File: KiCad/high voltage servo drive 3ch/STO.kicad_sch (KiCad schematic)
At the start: 34 parts, among them J8 STO, Q1 BSS83P, U15 PC-817S1-CTP1-F, U16 PC-817S1-CTP1-F, U19 PC-817S1-CTP1-F

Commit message: prepare rev0.1 for manufacturing
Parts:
- C188, C189, C190: Generic Allowed? (none) -> yes; LCSC# (none) -> C105882; Manufacturer (none) -> YAGEO; Part number (none) -> CC0402KRX5R9BB104; cost (none) -> 0.003
- D34, D38, D48: LCSC# (none) -> C12765; Manufacturer onsemi -> LRC; Part number BAT54SLT1G -> LBAT54SLT1G; cost (none) -> 0.01
- D35, D37, D49: LCSC# (none) -> C5199207; Manufacturer SMC Diode Solutions -> ElecSuper; Part number SM712 -> CDSOT23-SM712-ES; cost (none) -> 0.03
- D36: value STO_CH_1 -> LED; Generic Allowed? (none) -> yes; LCSC# (none) -> C965807; Manufacturer (none) -> XINGLIGHT; Part number (none) -> XL-1608UBC-04; cost (none) -> 0.004
- D39: value STO_CH_2 -> LED; Generic Allowed? (none) -> yes; LCSC# (none) -> C965807; Manufacturer (none) -> XINGLIGHT; Part number (none) -> XL-1608UBC-04; cost (none) -> 0.004
- D50: value STO_FBK -> LED; Generic Allowed? (none) -> yes; LCSC# (none) -> C965807; Manufacturer (none) -> XINGLIGHT; Part number (none) -> XL-1608UBC-04; cost (none) -> 0.004
- J8: now not fitted
- Q1: Generic Allowed? (none) -> yes; LCSC# (none) -> C7472872; Manufacturer (none) -> TECH PUBLIC; Part number (none) -> BSS83P; cost (none) -> 0.06
- R128, R129, R130, R131, R134, R87, R88, R89, R90, R92, R93, R94, R95: Generic Allowed? (none) -> yes, 1% or better; LCSC# (none) -> C106235; Manufacturer (none) -> YAGEO; Part number (none) -> RC0402FR-071KL; cost (none) -> 0.0007
- R132, R133, R91, R96: Generic Allowed? (none) -> yes; LCSC# (none) -> C60490; Manufacturer (none) -> YAGEO; Part number (none) -> RC0402FR-0710KL; cost (none) -> 0.0007
- U15, U16, U19: Manufacturer (none) -> HENGTUO; Part number (none) -> PC-817S1-CTP1-F; cost (none) -> 0.03

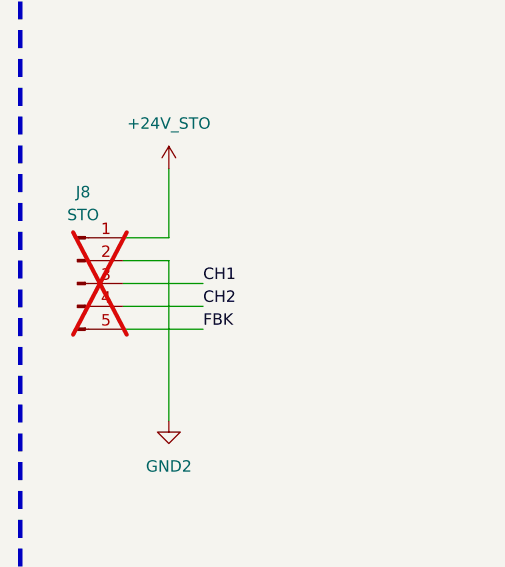
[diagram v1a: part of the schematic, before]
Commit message: update BOM and change transceivers
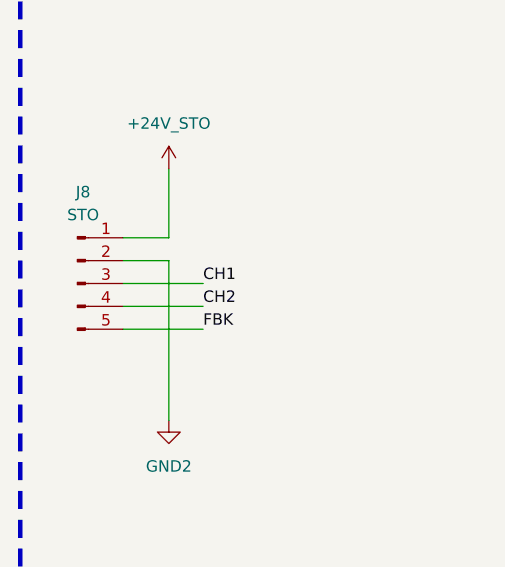
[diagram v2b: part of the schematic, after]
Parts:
- J8: now fitted
- U15, U16, U19: footprint Package_DIP:DIP-4_W7.62mm_SMDSocket_SmallPads -> Package_DIP:DIP-4_W7.62mm; Generic Allowed? (none) -> yes
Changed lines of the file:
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@@
 		(in_bom yes)
 		(on_board yes)
-		(dnp yes)
+		(dnp no)
 		(fields_autoplaced yes)
 		(property "Reference" "J8"
@@
 			)
 		)
-		(property "Description" "50v"
+		(property "Description" "Unpolarized capacitor"
 			(at 227.33 177.8 0)
 			(effects
@@
 			)
 		)
-		(property "Footprint" "Package_DIP:DIP-4_W7.62mm_SMDSocket_SmallPads"
+		(property "Footprint" "Package_DIP:DIP-4_W7.62mm"
 			(at 256.54 100.33 0)
 			(effects
@@
 			)
 		)
-		(property "Datasheet" ""
+		(property "Datasheet" "http://www.everlight.com/file/ProductFile/EL817.pdf"
 			(at 261.62 95.25 0)
 			(effects
@@
 			)
 		)
-		(property "Description" ""
+		(property "Description" "DC Optocoupler, Vce 35V, DIP-4"
 			(at 261.62 95.25 0)
 			(effects
@@
 		)
 		(property "cost" "0.03"
+			(at 261.62 95.25 0)
+			(effects
+				(font
+					(size 1.27 1.27)
+				)
+				(hide yes)
+			)
+		)
+		(property "Generic Allowed?" "yes"
 			(at 261.62 95.25 0)
 			(effects
@@
 			)
 		)
-		(property "Description" "50v"
+		(property "Description" "Unpolarized capacitor"
 			(at 198.12 81.28 0)
 			(effects
@@
 			)
 		)
-		(property "Description" "50v"
+		(property "Description" "Unpolarized capacitor"
 			(at 198.12 133.35 0)
 			(effects
@@
 			)
 		)
-		(property "Footprint" "Package_DIP:DIP-4_W7.62mm_SMDSocket_SmallPads"
+		(property "Footprint" "Package_DIP:DIP-4_W7.62mm"
 			(at 256.54 152.4 0)
 			(effects
@@
 			)
 		)
-		(property "Datasheet" ""
+		(property "Datasheet" "http://www.everlight.com/file/ProductFile/EL817.pdf"
 			(at 261.62 147.32 0)
 			(effects
@@
 			)
 		)
-		(property "Description" ""
+		(property "Description" "DC Optocoupler, Vce 35V, DIP-4"
 			(at 261.62 147.32 0)
 			(effects
@@
 		)
 		(property "cost" "0.03"
+			(at 261.62 147.32 0)
+			(effects
+				(font
+					(size 1.27 1.27)
+				)
+				(hide yes)
+			)
+		)
+		(property "Generic Allowed?" "yes"
 			(at 261.62 147.32 0)
 			(effects
@@
 			)
 		)
-		(property "Footprint" "Package_DIP:DIP-4_W7.62mm_SMDSocket_SmallPads"
+		(property "Footprint" "Package_DIP:DIP-4_W7.62mm"
 			(at 266.7 203.2 0)
 			(effects
@@
 			)
 		)
-		(property "Datasheet" ""
+		(property "Datasheet" "http://www.everlight.com/file/ProductFile/EL817.pdf"
 			(at 261.62 198.12 0)
 			(effects
@@
 			)
 		)
-		(property "Description" ""
+		(property "Description" "DC Optocoupler, Vce 35V, DIP-4"
 			(at 261.62 198.12 0)
 			(effects
@@
 			(at 261.62 198.12 0)
 			(effects
+				(font
+					(size 1.27 1.27)
+				)
+				(hide yes)
+			)
+		)
+		(property "Generic Allowed?" "yes"
+			(at 261.62 198.12 0)
+			(effects
